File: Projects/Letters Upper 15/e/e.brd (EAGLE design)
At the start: 16.5 x 21.6 mm, 37 parts

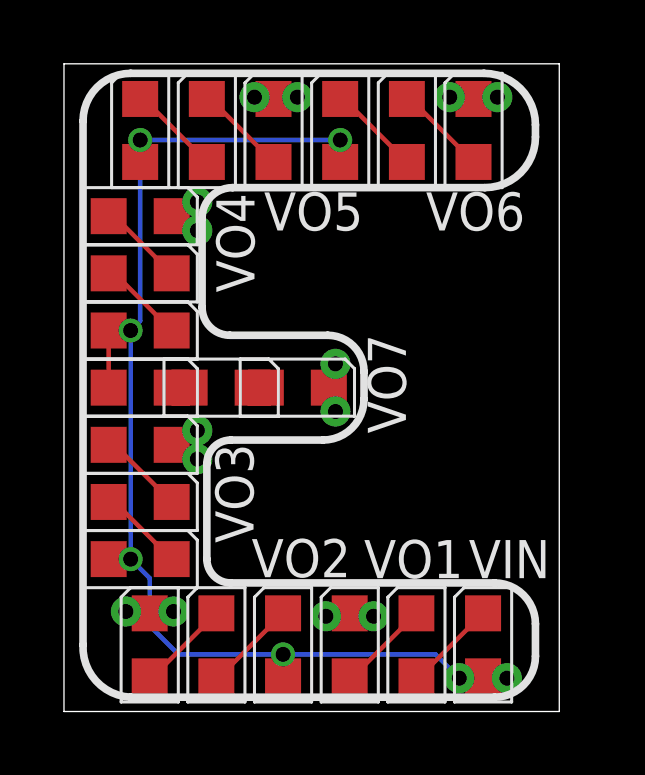
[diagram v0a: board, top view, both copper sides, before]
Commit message: 
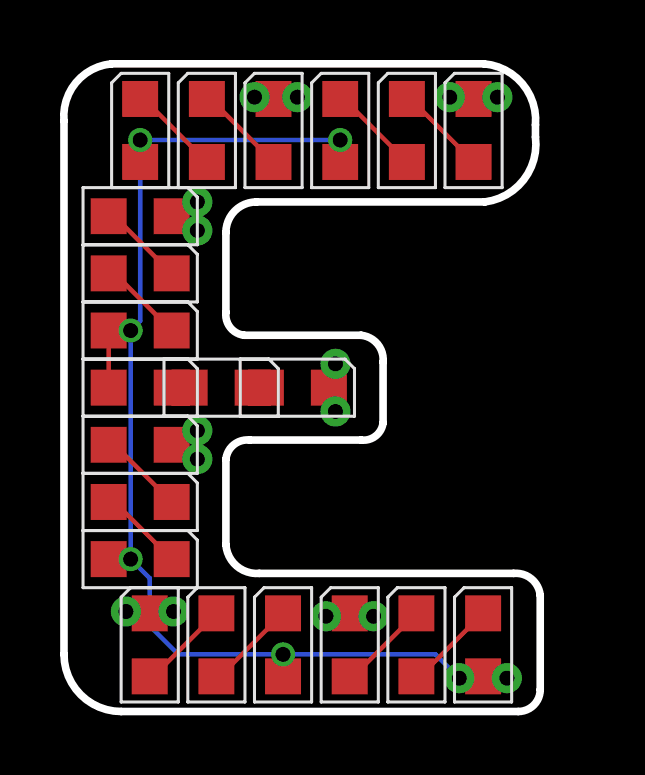
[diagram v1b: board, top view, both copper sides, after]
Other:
- board size 16.5 x 21.6 mm -> 15.9 x 21.6 mm
